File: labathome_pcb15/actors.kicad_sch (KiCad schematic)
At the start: 39 parts, among them J18 K1, J24 K1, J7 FAN5V, J8 GN 5V RGB GN, K1 G6K-2, Q1 BC817, Q2 IRLML6344, Q3 TIP41, Q4 BC817, Q5 IRLML6344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

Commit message: labathome_pcb15 ready for first review
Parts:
- removed R34: 3k3, Resistor_SMD:R_1206_3216Metric, symbol Device:R
- added R6: k22, Resistor_SMD:R_0402_1005Metric, symbol Device:R
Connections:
- net +24V: no longer D14.2 (A)
- net GND: now also R6.1
- net HEATER: now also D14.2 (A)
- net at D14.1 (K): now also R6.2
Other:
- moved on the sheet: C45, C46, C47, C48, D14, D15, D16, D17, D18, J7, J8, Q2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

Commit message: labathome_pcb15
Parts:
- D14: footprint LED_SMD:LED_0805_2012Metric -> LED_SMD:LED_0805_2012Metric_Pad1.15x1.40mm_HandSolder
- D15, D16, D17, D18: footprint LED_SMD:LED_WS2812B_PLCC4_5.0x5.0mm_P3.2mm -> liebler_OPTO:WS2812b_handsolder
- R12: footprint Resistor_SMD:R_0603_1608Metric -> Resistor_SMD:R_0402_1005Metric
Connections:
- net +5V: now also J8.3 (Pin_3); no longer J8.1 (Pin_1)
- net GND: no longer J8.3 (Pin_3)
- new net +3V3: J8.1 (Pin_1)
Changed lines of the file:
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@@
 	)
 	(junction
-		(at 160.02 72.39)
-		(diameter 0)
-		(color 0 0 0 0)
-	)
-	(junction
 		(at 80.01 33.02)
 		(diameter 0)
@@
 	(wire
 		(pts
-			(xy 151.13 69.85) (xy 152.4 69.85)
-		)
-		(stroke
-			(width 0)
-			(type default)
-		)
-	)
-	(wire
-		(pts
 			(xy 33.02 68.58) (xy 38.1 68.58)
 		)
@@
 	(wire
 		(pts
-			(xy 80.01 35.56) (xy 80.01 33.02)
+			(xy 160.02 67.31) (xy 151.13 67.31)
 		)
 		(stroke
@@
 	(wire
 		(pts
-			(xy 113.03 77.47) (xy 97.79 77.47)
+			(xy 80.01 35.56) (xy 80.01 33.02)
 		)
 		(stroke
@@
 	(wire
 		(pts
-			(xy 17.78 81.28) (xy 25.4 81.28)
+			(xy 113.03 77.47) (xy 97.79 77.47)
 		)
 		(stroke
@@
 	(wire
 		(pts
-			(xy 128.27 77.47) (xy 113.03 77.47)
+			(xy 17.78 81.28) (xy 25.4 81.28)
 		)
 		(stroke
@@
 	(wire
 		(pts
-			(xy 152.4 69.85) (xy 152.4 67.31)
+			(xy 128.27 77.47) (xy 113.03 77.47)
 		)
 		(stroke
@@
 	(wire
 		(pts
-			(xy 152.4 67.31) (xy 160.02 67.31)
-		)
-		(stroke
-			(width 0)
-			(type default)
-		)
-	)
-	(wire
-		(pts
-			(xy 160.02 69.85) (xy 160.02 72.39)
+			(xy 128.27 77.47) (xy 143.51 77.47)
 		)
 		(stroke
@@
 	(wire
 		(pts
-			(xy 128.27 77.47) (xy 143.51 77.47)
+			(xy 27.94 78.74) (xy 27.94 81.28)
 		)
 		(stroke
@@
 	(wire
 		(pts
-			(xy 27.94 78.74) (xy 27.94 81.28)
+			(xy 72.39 29.21) (xy 72.39 31.75)
 		)
 		(stroke
@@
 	(wire
 		(pts
-			(xy 72.39 29.21) (xy 72.39 31.75)
+			(xy 80.01 25.4) (xy 90.17 25.4)
 		)
 		(stroke
@@
 	(wire
 		(pts
-			(xy 80.01 25.4) (xy 90.17 25.4)
+			(xy 72.39 39.37) (xy 72.39 40.64)
 		)
 		(stroke
@@
 	(wire
 		(pts
-			(xy 72.39 39.37) (xy 72.39 40.64)
+			(xy 151.13 67.31) (xy 151.13 69.85)
 		)
 		(stroke
@@
 			)
 		)
-		(property "Footprint" "Resistor_SMD:R_0603_1608Metric"
+		(property "Footprint" "Resistor_SMD:R_0402_1005Metric"
 			(at 43.18 31.242 90)
 			(effects
@@
 			)
 		)
-		(property "Footprint" "LED_SMD:LED_0805_2012Metric"
+		(property "Footprint" "LED_SMD:LED_0805_2012Metric_Pad1.15x1.40mm_HandSolder"
 			(at 17.78 69.85 0)
 			(effects
@@
 	(symbol
 		(lib_id "power:+5V")
-		(at 160.02 64.77 90)
+		(at 160.02 69.85 90)
 		(unit 1)
 		(exclude_from_sim no)
@@
 		(dnp no)
 		(property "Reference" "#PWR0104"
-			(at 163.83 64.77 0)
+			(at 163.83 69.85 0)
 			(effects
 				(font
@@
 		)
 		(property "Value" "+5V"
-			(at 157.48 64.77 90)
+			(at 157.48 69.85 90)
 			(effects
 				(font
@@
 		)
 		(property "Footprint" ""
-			(at 160.02 64.77 0)
+			(at 160.02 69.85 0)
 			(effects
 				(font
@@
 		)
 		(property "Datasheet" ""
-			(at 160.02 64.77 0)
+			(at 160.02 69.85 0)
 			(effects
 				(font
@@
 		)
 		(property "Description" ""
-			(at 160.02 64.77 0)
+			(at 160.02 69.85 0)
 			(effects
 				(font
@@
 			)
 		)
-		(property "Footprint" "LED_SMD:LED_WS2812B_PLCC4_5.0x5.0mm_P3.2mm"
+		(property "Footprint" "liebler_OPTO:WS2812b_handsolder"
 			(at 144.78 77.47 0)
 			(effects
@@
 	)
 	(symbol
+		(lib_id "power:+3V3")
+		(at 160.02 64.77 90)
+		(unit 1)
+		(exclude_from_sim no)
+		(in_bom yes)
+		(on_board yes)
+		(dnp no)
+		(property "Reference" "#PWR0200"
+			(at 163.83 64.77 0)
+			(effects
+				(font
+					(size 1.27 1.27)
+				)
+				(hide yes)
+			)
+		)
+		(property "Value" "+3V3"
+			(at 157.48 64.77 90)
+			(effects
+				(font
+					(size 1.27 1.27)
+				)
+				(justify left)
+			)
+		)
+		(property "Footprint" ""
+			(at 160.02 64.77 0)
+			(effects
+				(font
+					(size 1.27 1.27)
+				)
+				(hide yes)
+			)
+		)
+		(property "Datasheet" ""
+			(at 160.02 64.77 0)
+			(effects
+				(font
+					(size 1.27 1.27)
+				)
+				(hide yes)
+			)
+		)
+		(property "Description" "Power symbol creates a global label with name \"+3V3\""
+			(at 160.02 64.77 0)
+			(effects
+				(font
+					(size 1.27 1.27)
+				)
+				(hide yes)
+			)
+		)
+		(pin "1"
+		)
+		(instances
+			(project ""
+				(path "/e4d6926a-1a8b-424d-97c4-66b6ad87e4ac/7cc4a29d-fb70-4313-b60c-aaf23d93fc45"
+					(reference "#PWR0200")
+					(unit 1)
+				)
+			)
+		)
+	)
+	(symbol
 		(lib_id "LED:WS2812B")
 		(at 97.79 69.85 0)
@@
 			)
 		)
-		(property "Footprint" "LED_SMD:LED_WS2812B_PLCC4_5.0x5.0mm_P3.2mm"
+		(property "Footprint" "liebler_OPTO:WS2812b_handsolder"
 			(at 99.06 77.47 0)
 			(effects
@@
 			)
 		)
-		(property "Footprint" "LED_SMD:LED_WS2812B_PLCC4_5.0x5.0mm_P3.2mm"
+		(property "Footprint" "liebler_OPTO:WS2812b_handsolder"
 			(at 129.54 77.47 0)
 			(effects
@@
 			)
 		)
-		(property "Footprint" "LED_SMD:LED_WS2812B_PLCC4_5.0x5.0mm_P3.2mm"
+		(property "Footprint" "liebler_OPTO:WS2812b_handsolder"
 			(at 114.3 77.47 0)
 			(effects

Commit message: labathome_pcb5 ready for review, 2nd
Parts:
- removed DRAWING2: Glasses, liebler_DRAWINGS:googles, symbol Mechanical:Fiducial
- removed DRAWING3: Hot, liebler_DRAWINGS:hot, symbol Mechanical:Fiducial
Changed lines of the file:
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@@
-	)
-	(symbol
-		(lib_id "Mechanical:Fiducial")
-		(at 144.78 95.25 0)
-		(unit 1)
-		(exclude_from_sim yes)
-		(in_bom no)
-		(on_board yes)
-		(dnp no)
-		(fields_autoplaced yes)
-		(property "Reference" "DRAWING3"
-			(at 147.32 93.9799 0)
-			(effects
-				(font
-					(size 1.27 1.27)
-				)
-				(justify left)
-			)
-		)
-		(property "Value" "Hot"
-			(at 147.32 96.5199 0)
-			(effects
-				(font
-					(size 1.27 1.27)
-				)
-				(justify left)
-			)
-		)
-		(property "Footprint" "liebler_DRAWINGS:hot"
-			(at 144.78 95.25 0)
-			(effects
-				(font
-					(size 1.27 1.27)
-				)
-				(hide yes)
-			)
-		)
-		(property "Datasheet" "~"
-			(at 144.78 95.25 0)
-			(effects
-				(font
-					(size 1.27 1.27)
-				)
-				(hide yes)
-			)
-		)
-		(property "Description" "Fiducial Marker"
-			(at 144.78 95.25 0)
-			(effects
-				(font
-					(size 1.27 1.27)
-				)
-				(hide yes)
-			)
-		)
-		(instances
-			(project "labathome_pcb15"
-				(path "/e4d6926a-1a8b-424d-97c4-66b6ad87e4ac/7cc4a29d-fb70-4313-b60c-aaf23d93fc45"
-					(reference "DRAWING3")
-					(unit 1)
-				)
-			)
-		)
-	)
-	(symbol
-		(lib_id "Mechanical:Fiducial")
-		(at 144.78 88.9 0)
-		(unit 1)
-		(exclude_from_sim yes)
-		(in_bom no)
-		(on_board yes)
-		(dnp no)
-		(fields_autoplaced yes)
-		(property "Reference" "DRAWING2"
-			(at 147.32 87.6299 0)
-			(effects
-				(font
-					(size 1.27 1.27)
-				)
-				(justify left)
-			)
-		)
-		(property "Value" "Glasses"
-			(at 147.32 90.1699 0)
-			(effects
-				(font
-					(size 1.27 1.27)
-				)
-				(justify left)
-			)
-		)
-		(property "Footprint" "liebler_DRAWINGS:googles"
-			(at 144.78 88.9 0)
-			(effects
-				(font
-					(size 1.27 1.27)
-				)
-				(hide yes)
-			)
-		)
-		(property "Datasheet" "~"
-			(at 144.78 88.9 0)
-			(effects
-				(font
-					(size 1.27 1.27)
-				)
-				(hide yes)
-			)
-		)
-		(property "Description" "Fiducial Marker"
-			(at 144.78 88.9 0)
-			(effects
-				(font
-					(size 1.27 1.27)
-				)
-				(hide yes)
-			)
-		)
-		(instances
-			(project ""
-				(path "/e4d6926a-1a8b-424d-97c4-66b6ad87e4ac/7cc4a29d-fb70-4313-b60c-aaf23d93fc45"
-					(reference "DRAWING2")
-					(unit 1)
-				)
-			)
-		)
 	)
 	(symbol

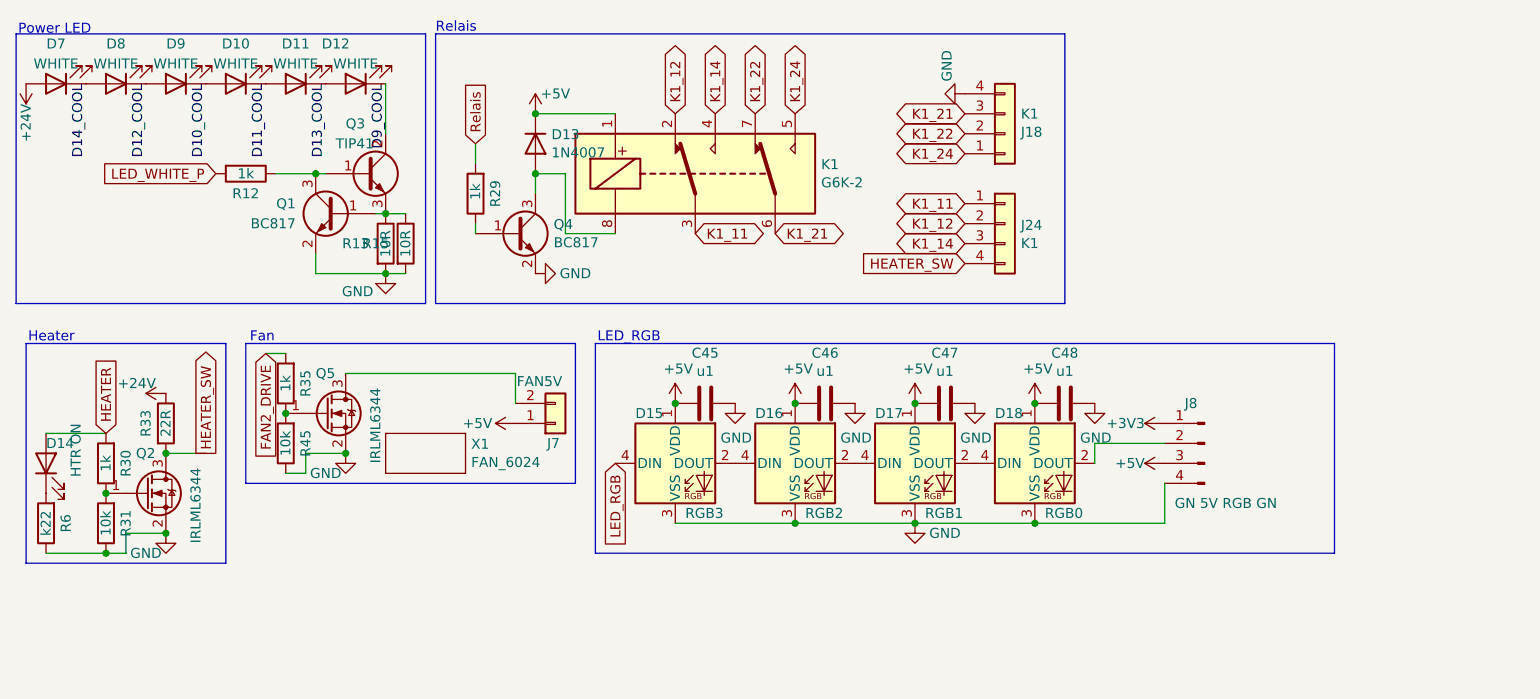
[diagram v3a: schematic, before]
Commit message: Various PCB and Code updates after review from Jana Marie Hemsing. Big Thankyou
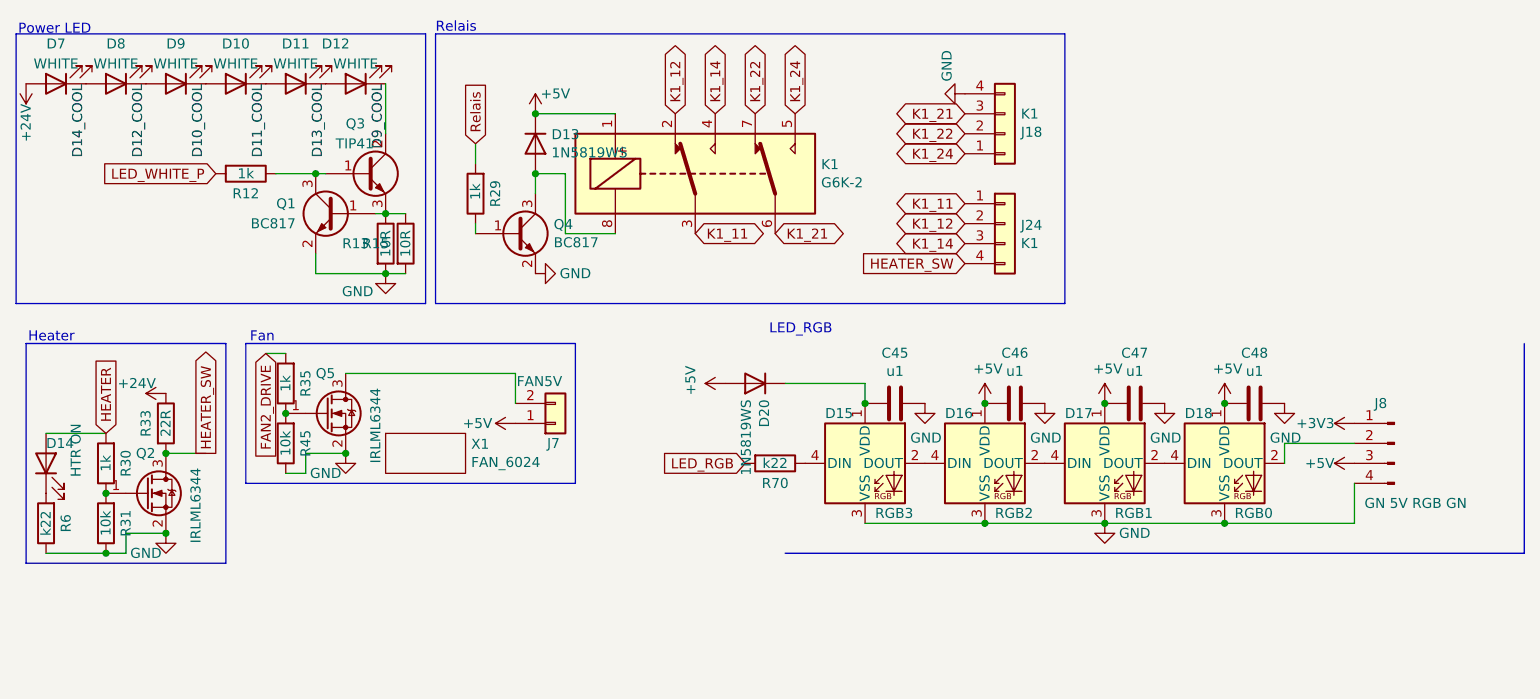
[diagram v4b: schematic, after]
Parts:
- added D20: 1N5819WS, Diode_SMD:D_SOD-323, symbol Device:D
- added R70: k22, Resistor_SMD:R_0402_1005Metric, symbol Device:R
- D13: value 1N4007 -> 1N5819WS; footprint Diode_SMD:D_SOD-123 -> Diode_SMD:D_SOD-323
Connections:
- net +5V: now also D20.2 (A); no longer C45.2, D15.1 (VDD)
- net LED_RGB: now also R70.2; no longer D15.4 (DIN)
- new net: D15.4 (DIN), R70.1
- new net: C45.2, D15.1 (VDD), D20.1 (K)
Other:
- moved on the sheet: C45, C46, C47, C48, D15, D16, D17, D18, J8

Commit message: Further improventents in PCB layout
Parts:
- J8: symbol Connector:Conn_01x04_Male -> Connector_Generic:Conn_01x04
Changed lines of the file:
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@@
 			)
 		)
-		(property "Description" ""
+		(property "Description" "Power symbol creates a global label with name \"+24V\""
 			(at 15.24 21.59 0)
 			(effects
@@
 			)
 		)
-		(property "Description" ""
+		(property "Description" "Power symbol creates a global label with name \"GND\" , ground"
 			(at 80.01 45.72 0)
 			(effects
@@
 	)
 	(symbol
-		(lib_id "Connector:Conn_01x04_Male")
+		(lib_id "Connector_Generic:Conn_01x04")
 		(at 189.23 67.31 0)
-		(mirror y)
 		(unit 1)
 		(exclude_from_sim no)
@@
 		(dnp no)
 		(property "Reference" "J8"
-			(at 186.69 62.23 0)
+			(at 191.77 62.23 0)
 			(effects
 				(font
@@
 		)
 		(property "Value" "GN 5V RGB GN"
-			(at 185.42 74.93 0)
+			(at 193.04 74.93 0)
 			(effects
 				(font
@@
 			)
 		)
-		(property "Description" ""
+		(property "Description" "Generic connector, single row, 01x04, script generated (kicad-library-utils/schlib/autogen/connector/)"
 			(at 189.23 67.31 0)
 			(effects
@@
 			)
 		)
-		(property "Description" ""
+		(property "Description" "Power symbol creates a global label with name \"GND\" , ground"
 			(at 175.26 62.23 0)
 			(effects
@@
 			)
 		)
-		(property "Description" ""
+		(property "Description" "Power symbol creates a global label with name \"+5V\""
 			(at 184.15 69.85 0)
 			(effects
@@
 			)
 		)
-		(property "Description" ""
+		(property "Description" "5.3A Id, 30V Vds, 27mOhm Rds, N-Channel HEXFET Power MOSFET, SOT-23"
 			(at 53.34 63.5 0)
 			(effects
@@
 			)
 		)
-		(property "Description" ""
+		(property "Description" "Power symbol creates a global label with name \"GND\" , ground"
 			(at 60.96 45.72 0)
 			(effects
@@
 			)
 		)
-		(property "Description" ""
+		(property "Description" "Power symbol creates a global label with name \"GND\" , ground"
 			(at 129.54 62.23 0)
 			(effects
@@
 			)
 		)
-		(property "Description" ""
+		(property "Description" "5.3A Id, 30V Vds, 27mOhm Rds, N-Channel HEXFET Power MOSFET, SOT-23"
 			(at 30.48 73.66 0)
 			(effects
@@
 			)
 		)
-		(property "Description" ""
+		(property "Description" "Power symbol creates a global label with name \"+5V\""
 			(at 152.4 62.23 0)
 			(effects
@@
 			)
 		)
-		(property "Description" ""
+		(property "Description" "Power symbol creates a global label with name \"GND\" , ground"
 			(at 33.02 78.74 0)
 			(effects
@@
 			)
 		)
-		(property "Description" ""
+		(property "Description" "Power symbol creates a global label with name \"+5V\""
 			(at 104.14 59.69 0)
 			(effects
@@
 			)
 		)
-		(property "Description" ""
+		(property "Description" "Power symbol creates a global label with name \"+5V\""
 			(at 80.01 25.4 0)
 			(effects
@@
 			)
 		)
-		(property "Description" ""
+		(property "Description" "Diode"
+			(at 80.01 29.21 0)
+			(effects
+				(font
+					(size 1.27 1.27)
+				)
+				(hide yes)
+			)
+		)
+		(property "Sim.Device" "D"
+			(at 80.01 29.21 0)
+			(effects
+				(font
+					(size 1.27 1.27)
+				)
+				(hide yes)
+			)
+		)
+		(property "Sim.Pins" "1=K 2=A"
 			(at 80.01 29.21 0)
 			(effects
@@
 			)
 		)
-		(property "Description" ""
+		(property "Description" "Power symbol creates a global label with name \"GND\" , ground"
 			(at 134.62 22.86 0)
 			(effects
@@
 			)
 		)
-		(property "Description" ""
+		(property "Description" "Power symbol creates a global label with name \"+5V\""
 			(at 137.16 62.23 0)
 			(effects
@@
 			)
 		)
-		(property "Description" ""
+		(property "Description" "Power symbol creates a global label with name \"+5V\""
 			(at 167.64 62.23 0)
 			(effects
@@
 			)
 		)
-		(property "Description" ""
+		(property "Description" "Power symbol creates a global label with name \"+24V\""
 			(at 33.02 60.96 0)
 			(effects
@@
 			)
 		)
-		(property "Description" ""
+		(property "Description" "Power symbol creates a global label with name \"GND\" , ground"
 			(at 55.88 68.58 0)
 			(effects
@@
 			)
 		)
-		(property "Description" ""
+		(property "Description" "Power symbol creates a global label with name \"GND\" , ground"
 			(at 152.4 77.47 0)
 			(effects
@@
 			)
 		)
-		(property "Description" ""
+		(property "Description" "Power symbol creates a global label with name \"GND\" , ground"
 			(at 144.78 62.23 0)
 			(effects
@@
 			)
 		)
-		(property "Description" ""
+		(property "Description" "Power symbol creates a global label with name \"GND\" , ground"
 			(at 160.02 62.23 0)
 			(effects
@@
 			)
 		)
-		(property "Description" ""
+		(property "Description" "Power symbol creates a global label with name \"+5V\""
 			(at 77.47 64.77 0)
 			(effects
@@
 			)
 		)
-		(property "Description" ""
+		(property "Description" "Diode"
+			(at 107.95 59.69 0)
+			(effects
+				(font
+					(size 1.27 1.27)
+				)
+				(hide yes)
+			)
+		)
+		(property "Sim.Device" "D"
+			(at 107.95 59.69 0)
+			(effects
+				(font
+					(size 1.27 1.27)
+				)
+				(hide yes)
+			)
+		)
+		(property "Sim.Pins" "1=K 2=A"
 			(at 107.95 59.69 0)
 			(effects

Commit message: lbathome 15.1
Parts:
- J8: value GN 5V RGB GN -> 3V GN RGB 5V
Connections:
- net +5V: now also J8.4 (Pin_4); no longer J8.3 (Pin_3)
- net GND: now also J8.2 (Pin_2); no longer J8.4 (Pin_4)
- net at D18.2 (DOUT): now also J8.3 (Pin_3); no longer J8.2 (Pin_2)
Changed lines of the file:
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@@
 	(wire
 		(pts
-			(xy 184.15 77.47) (xy 184.15 72.39)
-		)
-		(stroke
-			(width 0)
-			(type default)
-		)
-	)
-	(wire
-		(pts
 			(xy 46.99 33.02) (xy 52.07 33.02)
 		)
@@
 	(wire
 		(pts
-			(xy 184.15 67.31) (xy 175.26 67.31)
-		)
-		(stroke
-			(width 0)
-			(type default)
-		)
-	)
-	(wire
-		(pts
 			(xy 80.01 35.56) (xy 80.01 33.02)
 		)
@@
 	(wire
 		(pts
-			(xy 152.4 77.47) (xy 167.64 77.47)
+			(xy 175.26 69.85) (xy 184.15 69.85)
 		)
 		(stroke
@@
 	(wire
 		(pts
-			(xy 27.94 78.74) (xy 27.94 81.28)
+			(xy 152.4 77.47) (xy 167.64 77.47)
 		)
 		(stroke
@@
 	(wire
 		(pts
-			(xy 72.39 29.21) (xy 72.39 31.75)
+			(xy 27.94 78.74) (xy 27.94 81.28)
 		)
 		(stroke
@@
 	(wire
 		(pts
-			(xy 80.01 25.4) (xy 90.17 25.4)
+			(xy 72.39 29.21) (xy 72.39 31.75)
 		)
 		(stroke
@@
 	(wire
 		(pts
-			(xy 72.39 39.37) (xy 72.39 40.64)
+			(xy 80.01 25.4) (xy 90.17 25.4)
 		)
 		(stroke
@@
 	(wire
 		(pts
-			(xy 175.26 67.31) (xy 175.26 69.85)
+			(xy 72.39 39.37) (xy 72.39 40.64)
 		)
 		(stroke
@@
 			)
 		)
-		(property "Value" "GN 5V RGB GN"
+		(property "Value" "3V GN RGB 5V"
 			(at 193.04 74.93 0)
 			(effects
@@
 	)
 	(symbol
-		(lib_id "power:+5V")
-		(at 184.15 69.85 90)
-		(unit 1)
-		(exclude_from_sim no)
-		(in_bom yes)
-		(on_board yes)
-		(dnp no)
-		(property "Reference" "#PWR0104"
-			(at 187.96 69.85 0)
-			(effects
-				(font
-					(size 1.27 1.27)
-				)
-				(hide yes)
-			)
-		)
-		(property "Value" "+5V"
-			(at 181.61 69.85 90)
-			(effects
-				(font
-					(size 1.27 1.27)
-				)
-				(justify left)
-			)
-		)
-		(property "Footprint" ""
-			(at 184.15 69.85 0)
-			(effects
-				(font
-					(size 1.27 1.27)
-				)
-				(hide yes)
-			)
-		)
-		(property "Datasheet" ""
-			(at 184.15 69.85 0)
-			(effects
-				(font
-					(size 1.27 1.27)
-				)
-				(hide yes)
-			)
-		)
-		(property "Description" "Power symbol creates a global label with name \"+5V\""
-			(at 184.15 69.85 0)
-			(effects
-				(font
-					(size 1.27 1.27)
-				)
-				(hide yes)
-			)
-		)
-		(pin "1"
-		)
-		(instances
-			(project "labathome_pcb15"
-				(path "/e4d6926a-1a8b-424d-97c4-66b6ad87e4ac/7cc4a29d-fb70-4313-b60c-aaf23d93fc45"
-					(reference "#PWR0104")
-					(unit 1)
-				)
-			)
-		)
-	)
-	(symbol
 		(lib_id "Transistor_FET:IRLML0030")
 		(at 53.34 63.5 0)
@@
 	(symbol
 		(lib_id "power:GND")
+		(at 184.15 67.31 270)
+		(unit 1)
+		(exclude_from_sim no)
+		(in_bom yes)
+		(on_board yes)
+		(dnp no)
+		(property "Reference" "#PWR0104"
+			(at 177.8 67.31 0)
+			(effects
+				(font
+					(size 1.27 1.27)
+				)
+				(hide yes)
+			)
+		)
+		(property "Value" "GND"
+			(at 179.578 67.31 90)
+			(effects
+				(font
+					(size 1.27 1.27)
+				)
+			)
+		)
+		(property "Footprint" ""
+			(at 184.15 67.31 0)
+			(effects
+				(font
+					(size 1.27 1.27)
+				)
+				(hide yes)
+			)
+		)
+		(property "Datasheet" ""
+			(at 184.15 67.31 0)
+			(effects
+				(font
+					(size 1.27 1.27)
+				)
+				(hide yes)
+			)
+		)
+		(property "Description" "Power symbol creates a global label with name \"GND\" , ground"
+			(at 184.15 67.31 0)
+			(effects
+				(font
+					(size 1.27 1.27)
+				)
+				(hide yes)
+			)
+		)
+		(pin "1"
+		)
+		(instances
+			(project "labathome_pcb15"
+				(path "/e4d6926a-1a8b-424d-97c4-66b6ad87e4ac/7cc4a29d-fb70-4313-b60c-aaf23d93fc45"
+					(reference "#PWR0104")
+					(unit 1)
+				)
+			)
+		)
+	)
+	(symbol
+		(lib_id "power:GND")
 		(at 134.62 22.86 270)
 		(unit 1)
@@
 					(unit 1)
 				)
+			)
+		)
+	)
+	(symbol
+		(lib_id "power:+5V")
+		(at 184.15 72.39 90)
+		(unit 1)
+		(exclude_from_sim no)
+		(in_bom yes)
+		(on_board yes)
+		(dnp no)
+		(property "Reference" "#PWR0122"
+			(at 187.96 72.39 0)
+			(effects
+				(font
+					(size 1.27 1.27)
+				)
+				(hide yes)
+			)
+		)
+		(property "Value" "+5V"
+			(at 179.7558 72.009 90)
+			(effects
+				(font
+					(size 1.27 1.27)
+				)
+			)
+		)
+		(property "Footprint" ""
+			(at 184.15 72.39 0)
+			(effects
+				(font
+					(size 1.27 1.27)
+				)
+				(hide yes)
+			)
+		)
+		(property "Datasheet" ""
+			(at 184.15 72.39 0)
+			(effects
+				(font
+					(size 1.27 1.27)
+				)
+				(hide yes)
+			)
+		)
+		(property "Description" "Power symbol creates a global label with name \"+5V\""
+			(at 184.15 72.39 0)
+			(effects
+				(font
+					(size 1.27 1.27)
+				)
+				(hide yes)
+			)
+		)
+		(pin "1"
+		)
+		(instances
+			(project "labathome_pcb15"
+				(path "/e4d6926a-1a8b-424d-97c4-66b6ad87e4ac/7cc4a29d-fb70-4313-b60c-aaf23d93fc45"
+					(reference "#PWR0122")
+					(unit 1)
+				)
